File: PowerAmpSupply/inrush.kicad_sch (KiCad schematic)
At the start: 24 parts, among them Q5 SiR500DP, Q6 CMLDM7002AJ, U5 LTC3290

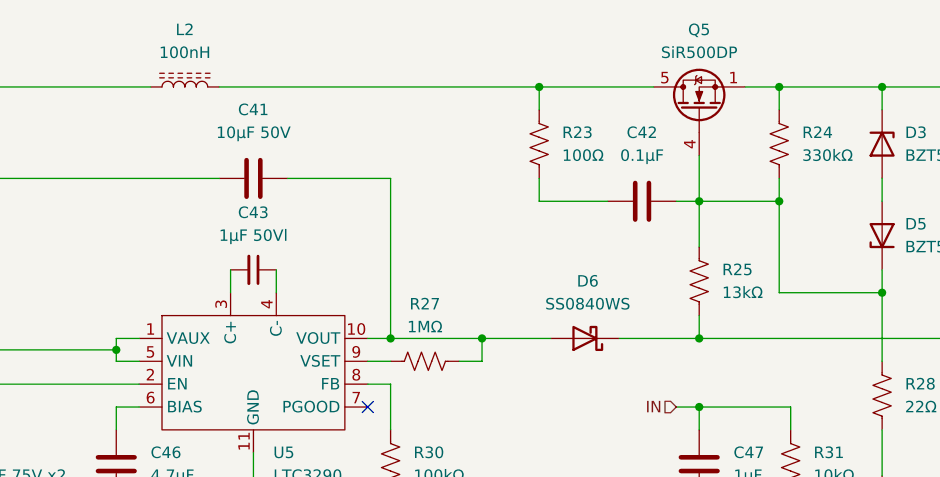
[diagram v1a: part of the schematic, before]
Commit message: PowerAmpSupply slower inrush applied and tested
Seems to work, so included the change in the design
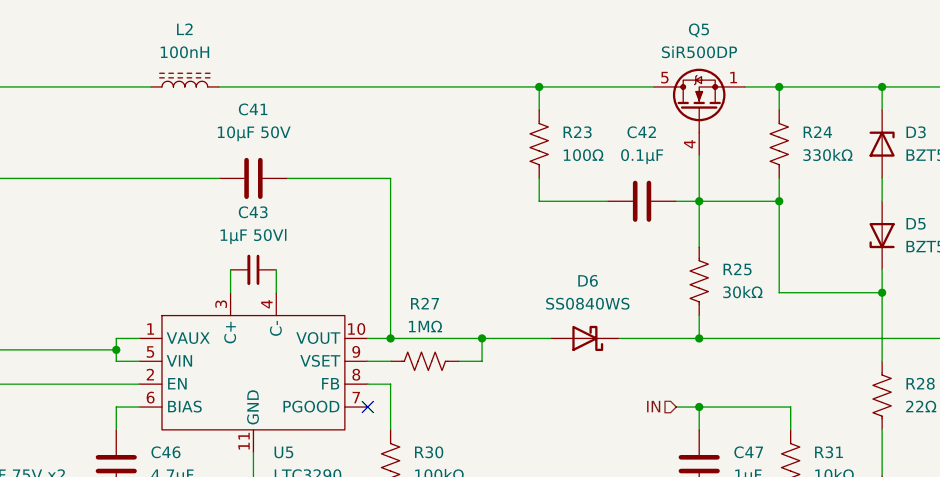
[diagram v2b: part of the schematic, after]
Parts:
- R25: value 13kΩ -> 30kΩ
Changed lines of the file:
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@@
 (kicad_sch
-	(version 20231120)
+	(version 20250114)
 	(generator "eeschema")
-	(generator_version "8.0")
+	(generator_version "9.0")
 	(paper "A4")
 	(junction
@@
 	(label "EN"
 		(at 180.34 116.84 180)
-		(fields_autoplaced yes)
 		(effects
 			(font
@@
 	(label "EN"
 		(at 71.12 93.98 180)
-		(fields_autoplaced yes)
 		(effects
 			(font
@@
 		(shape output)
 		(at 224.79 60.96 0)
-		(fields_autoplaced yes)
 		(effects
 			(font
@@
 		(shape input)
 		(at 58.42 60.96 180)
-		(fields_autoplaced yes)
 		(effects
 			(font
@@
 		(shape input)
 		(at 177.8 96.52 180)
-		(fields_autoplaced yes)
 		(effects
 			(font
@@
 			)
 		)
-		(property "Value" "13kΩ"
+		(property "Value" "30kΩ"
 			(at 182.88 83.8199 0)
 			(effects
